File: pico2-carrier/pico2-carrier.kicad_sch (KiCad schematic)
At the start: 27 parts, among them IC1 TFDU4101-TT3, IC2 M95512-DWDW4TP_K, IC3 W25Q128JVSIM_TR, SW1 RUN, SW2 BUT_L, SW3 BUT_M, SW4 BUT_R, U1 Pico 2

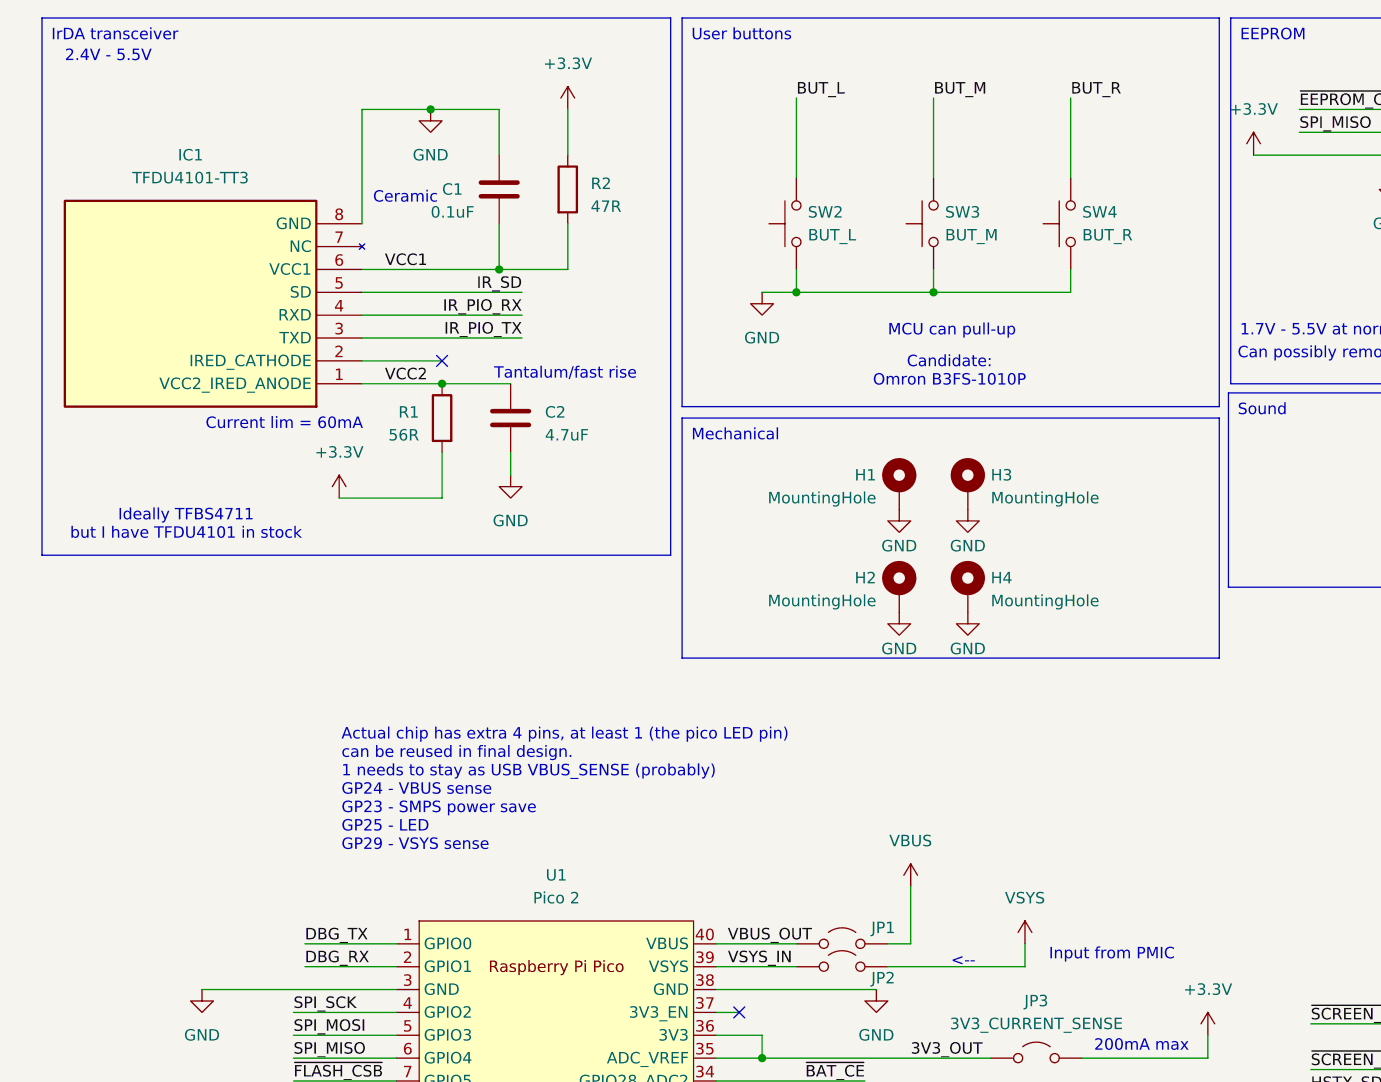
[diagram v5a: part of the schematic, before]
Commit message: carrier: add hardware button debounce
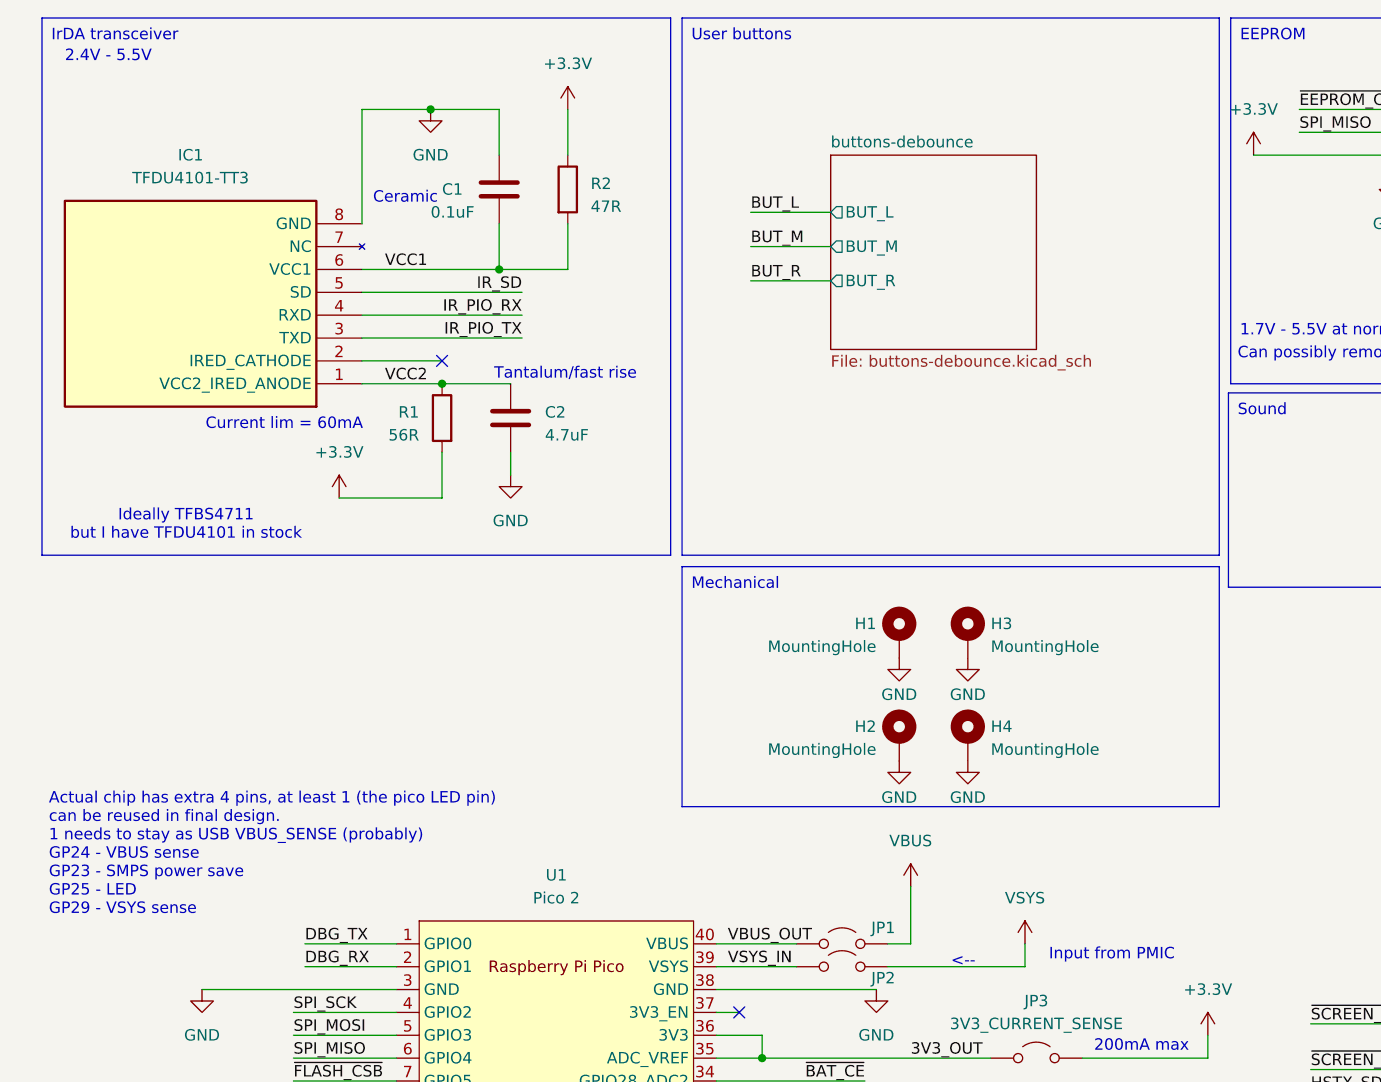
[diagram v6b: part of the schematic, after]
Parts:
- removed SW2: BUT_L, Button_Switch_SMD:SW_SPST_Omron_B3FS-101xP, symbol Switch:SW_Push
- removed SW3: BUT_M, Button_Switch_SMD:SW_SPST_Omron_B3FS-101xP, symbol Switch:SW_Push
- removed SW4: BUT_R, Button_Switch_SMD:SW_SPST_Omron_B3FS-101xP, symbol Switch:SW_Push
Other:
- added sheet buttons-debounce (buttons-debounce.kicad_sch)
- note removed: "Candidate: Omron B3FS-1010P"
- note removed: "MCU can pull-up"
- moved on the sheet: H1, H2, H3, H4

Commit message: carrier: add 3.3V zone, start tidying buttons, update caps to 0603
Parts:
- C2: footprint Capacitor_SMD:C_0402_1005Metric -> Capacitor_SMD:C_0603_1608Metric
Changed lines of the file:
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@@
 			)
 		)
-		(property "Footprint" "Capacitor_SMD:C_0402_1005Metric"
+		(property "Footprint" "Capacitor_SMD:C_0603_1608Metric"
 			(at 65.7352 60.96 0)
 			(effects

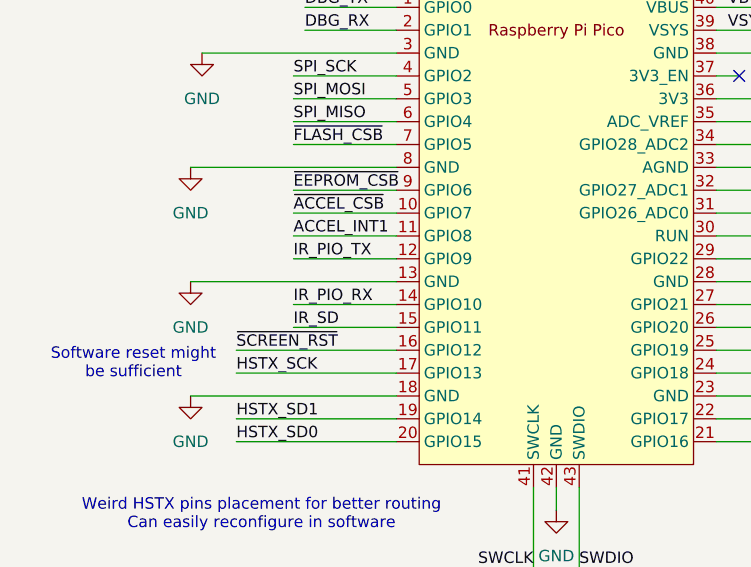
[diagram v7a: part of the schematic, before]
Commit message: carrier: update ir footprint
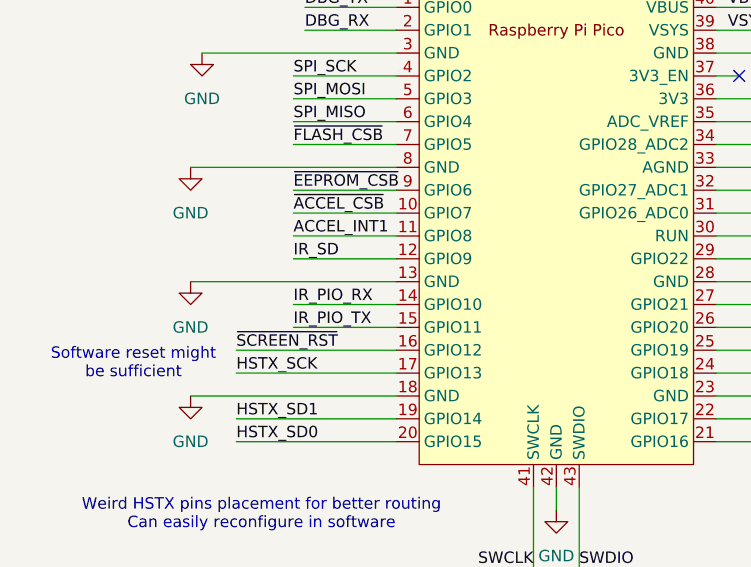
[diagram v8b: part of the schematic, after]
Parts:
- IC1: footprint SamacsysParts:TFDU4101-TR3 -> SamacsysParts:TFDU4101-TR3-Side
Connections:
- net IR_PIO_TX: now also U1.15 (GPIO11); no longer U1.12 (GPIO9)
- net IR_SD: now also U1.12 (GPIO9); no longer U1.15 (GPIO11)
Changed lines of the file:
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@@
-		)
-	)
-	(label "IR_PIO_TX"
-		(at 40.64 143.51 0)
-		(fields_autoplaced yes)
-		(effects
-			(font
-				(size 1.27 1.27)
-			)
-			(justify left bottom)
 		)
 	)
@@
 		)
 	)
-	(label "IR_SD"
-		(at 40.64 151.13 0)
-		(fields_autoplaced yes)
-		(effects
-			(font
-				(size 1.27 1.27)
-			)
-			(justify left bottom)
-		)
-	)
 	(label "I2C_SDA"
 		(at 205.74 143.51 0)
@@
 		)
 	)
+	(label "IR_SD"
+		(at 40.64 143.51 0)
+		(fields_autoplaced yes)
+		(effects
+			(font
+				(size 1.27 1.27)
+			)
+			(justify left bottom)
+		)
+	)
 	(label "VSYS_IN"
 		(at 153.67 149.86 0)
@@
 			)
 			(justify right bottom)
+		)
+	)
+	(label "IR_PIO_TX"
+		(at 40.64 151.13 0)
+		(fields_autoplaced yes)
+		(effects
+			(font
+				(size 1.27 1.27)
+			)
+			(justify left bottom)
 		)
 	)
@@
 			)
 		)
-		(property "Footprint" "SamacsysParts:TFDU4101-TR3"
+		(property "Footprint" "SamacsysParts:TFDU4101-TR3-Side"
 			(at 13.97 -41.58 0)
 			(effects
